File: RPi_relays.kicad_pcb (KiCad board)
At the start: 2 copper layers, 100 x 58.5 mm, 22 parts, among them J1 Raspberry_Pi_2_3, J3 Conn_01x03_Female, J4 Conn_01x03_Female, J5 Conn_01x03_Female, K1 G5Q-1, K2 G5Q-1, Q1 2N7002, Q2 2N7002

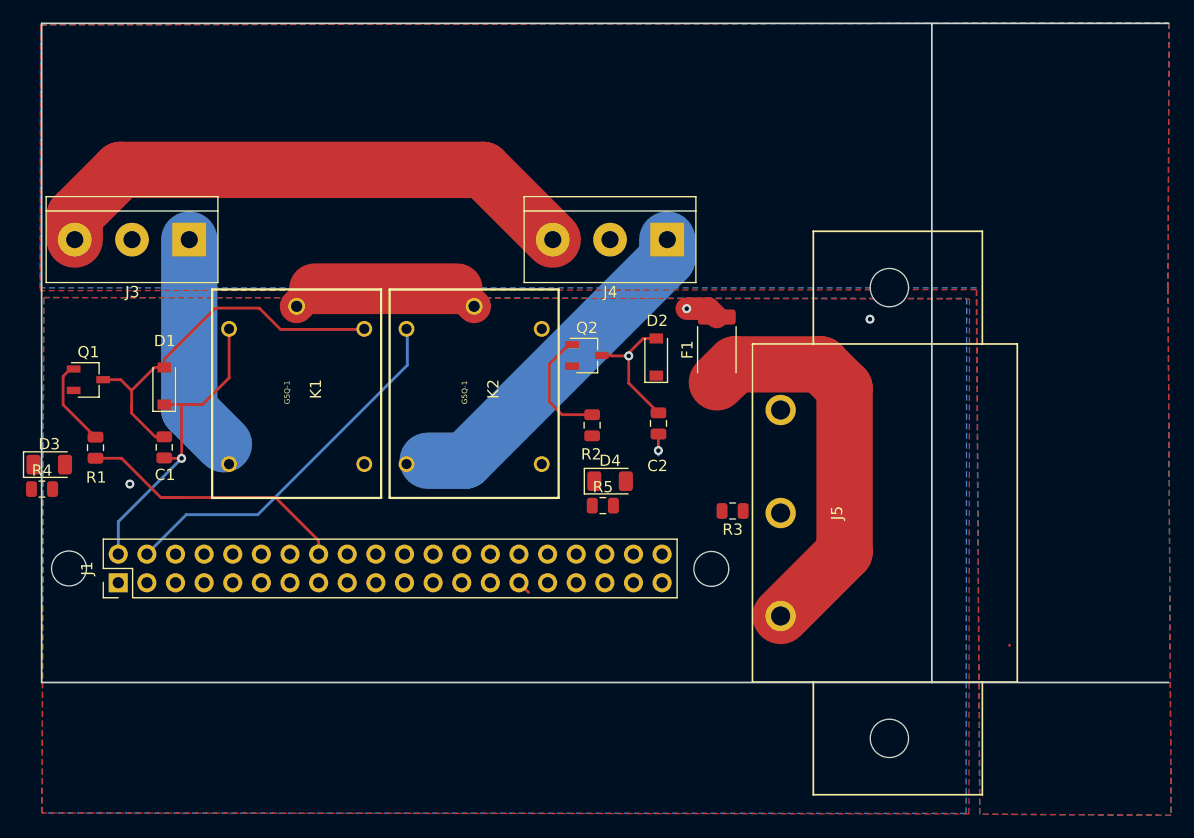
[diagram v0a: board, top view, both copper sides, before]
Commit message: Button added
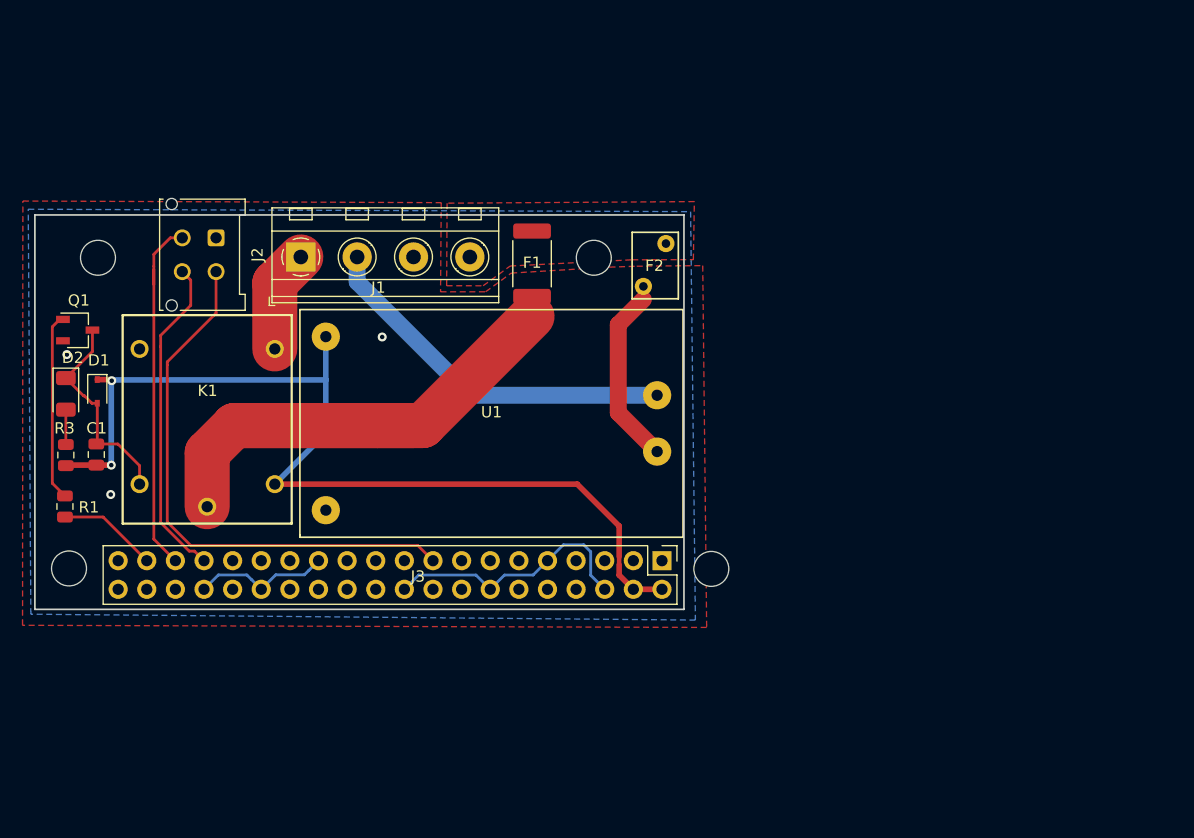
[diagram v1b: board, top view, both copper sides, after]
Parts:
- removed C2: 4.7uF, Capacitor_SMD:C_0805_2012Metric
- removed D3, D4: 2.4/25, LED_SMD:LED_1206_3216Metric
- removed the J3 at (113.1, 59.2)
- removed J4: Conn_01x03_Female, TerminalBlock:TerminalBlock_bornier-3_P5.08mm
- removed J5: Conn_01x03_Female, LP_connectors:PX0580_PC
- removed K2: G5Q-1, switches:SRD-05VDC-SL-C
- removed Q2: 2N7002, Package_TO_SOT_SMD:TSOT-23
- removed R2: 2K, Resistor_SMD:R_0805_2012Metric
- removed R4, R5: 100, Resistor_SMD:R_0805_2012Metric
- added F2: 50mA, Littelfuse:Littelfuse_LVR008NS, F.Cu at (153.4, 63.3)
- added G***: LOGO, logo:LOGO, F.Cu at (128.0, 75.6)
- added J1: PWR, TerminalBlock_MetzConnect:TerminalBlock_MetzConnect_Type094_RT03504HBLU_1x04_P5.00mm_Horizontal, F.Cu at (123.0, 60.7)
- added J2: Conn_01x04_Female, Connector_Molex:Molex_Micro-Fit_3.0_43045-0412_2x02_P3.00mm_Vertical, F.Cu at (115.5, 59.0)
- added REF**: M3 screw, LP_connectors:M3_screw, F.Cu at (149.0, 60.8)
- added REF**: M3 screw, LP_connectors:M3_screw, F.Cu at (105.0, 60.8)
- added U1: HLK-PMxx, Hi-Link:HLK-PM01, F.Cu at (139.9, 75.5)
- D1: footprint Diode_SMD:D_SOD-123 -> Diode_SMD:D_SOD-323
- D2: value B5818WS -> 2.4/25; footprint Diode_SMD:D_SOD-123 -> LED_SMD:LED_1206_3216Metric
- R1: value 2K -> 3K
- R3: value 10K -> 100
- moved R3 59.4 mm to (102.2, 78.3), turned to 90 degrees
- moved D2 52.5 mm to (102.2, 72.9), turned to 270 degrees
- moved J3 48.4 mm to (155.1, 90.2), turned to 270 degrees
- moved F1 18.1 mm to (143.5, 61.3)
- moved K1 8.71 mm to (114.6, 75.5), turned to 90 degrees
- moved C1 6.06 mm to (104.8, 78.3)
- moved D1 5.96 mm to (104.9, 72.7), turned to 270 degrees
- moved R1 5.88 mm to (102.1, 82.9)
- moved Q1 4.50 mm to (103.2, 67.2)
- renumbered J1 to J3
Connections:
- net D0 renamed Net-(J3-Pad26)
- net D1 renamed Net-(J3-Pad24)
- net D2 renamed Net-(J3-Pad21)
- net D3 renamed Net-(J3-Pad19)
- net D4 renamed Net-(J3-Pad23)
- net D5 renamed Net-(J3-Pad32)
- net D7 renamed Net-(J3-Pad8)
- net HREF renamed Net-(J3-Pad7)
- net PCLK renamed Net-(J3-Pad31)
- net PWDN renamed Net-(J3-Pad36)
- net RESET renamed Net-(J3-Pad10)
- net SCL renamed Net-(J3-Pad5)
- net SDA renamed Net-(J3-Pad3)
- net VSYNC renamed Net-(J3-Pad29)
- D2 pad 1: 5V -> Net-(C1-Pad2)
- D2 pad 2: Net-(C2-Pad2) -> Net-(D2-Pad2)
- F1 pad 1: Net-(F1-Pad1) -> AC_H
- F1 pad 2: AC_H -> Net-(F1-Pad2)
- J3 pad 1: 3V3 -> Net-(J3-Pad1)
- J3 pad 16: RELAY1 -> Net-(J3-Pad16)
- J3 pad 22: RELAY2 -> Net-(J3-Pad22)
- J3 pad 33: D6 -> DTRT_LED
- J3 pad 35: Net-(J1-Pad35) -> DTRT_SW
- J3 pad 37: Net-(J1-Pad37) -> RELAY1
- R3 pad 1: GND -> 5V
- R3 pad 2: Net-(J3-Pad2) -> Net-(D2-Pad2)
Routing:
- net 3V3: track 0.00 -> 49.0 mm
- net Net-(J3-Pad3) (its old number): track 48.8 -> 0.00 mm
- net GND: track 0.00 -> 35.6 mm, vias 2 -> 3
- net Net-(F1-Pad1): track 35.5 -> 0.00 mm
- net AC_H: track 21.1 -> 56.4 mm, vias 1 -> 0
- net DTRT_SW: track 0.00 -> 32.4 mm
- net Net-(J1-Pad2): track 0.00 -> 32.4 mm
- net AC_RELAY2: track 32.1 -> 0.00 mm
- net DTRT_LED: track 0.00 -> 28.9 mm
- net 5V: track 64.1 -> 87.8 mm
- net Net-(F2-Pad1): track 0.00 -> 17.0 mm
- net RELAY1: track 25.7 -> 8.86 mm
- net Net-(C1-Pad2): track 34.4 -> 19.0 mm
- net AC_RELAY1: track 21.4 -> 9.12 mm
- net Net-(C2-Pad2): track 12.0 -> 0.00 mm, vias 1 -> 0
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- added copper zone on F.Cu, net Net-(F1-Pad2)
- removed copper zone on B.Cu, net Net-(J3-Pad2)
- removed copper zone on F.Cu, net Net-(J3-Pad2)
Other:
- board size 100 x 58.5 mm -> 57.6 x 35 mm
- net class 5V added: clearance 0.2, trace_width 0.5, via_dia 0.8, via_drill 0.4
